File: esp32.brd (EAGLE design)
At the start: 59.2 x 57.2 mm, 14 parts, among them IC1 LM1117IMPX-3.3, U1 ESP32MOD

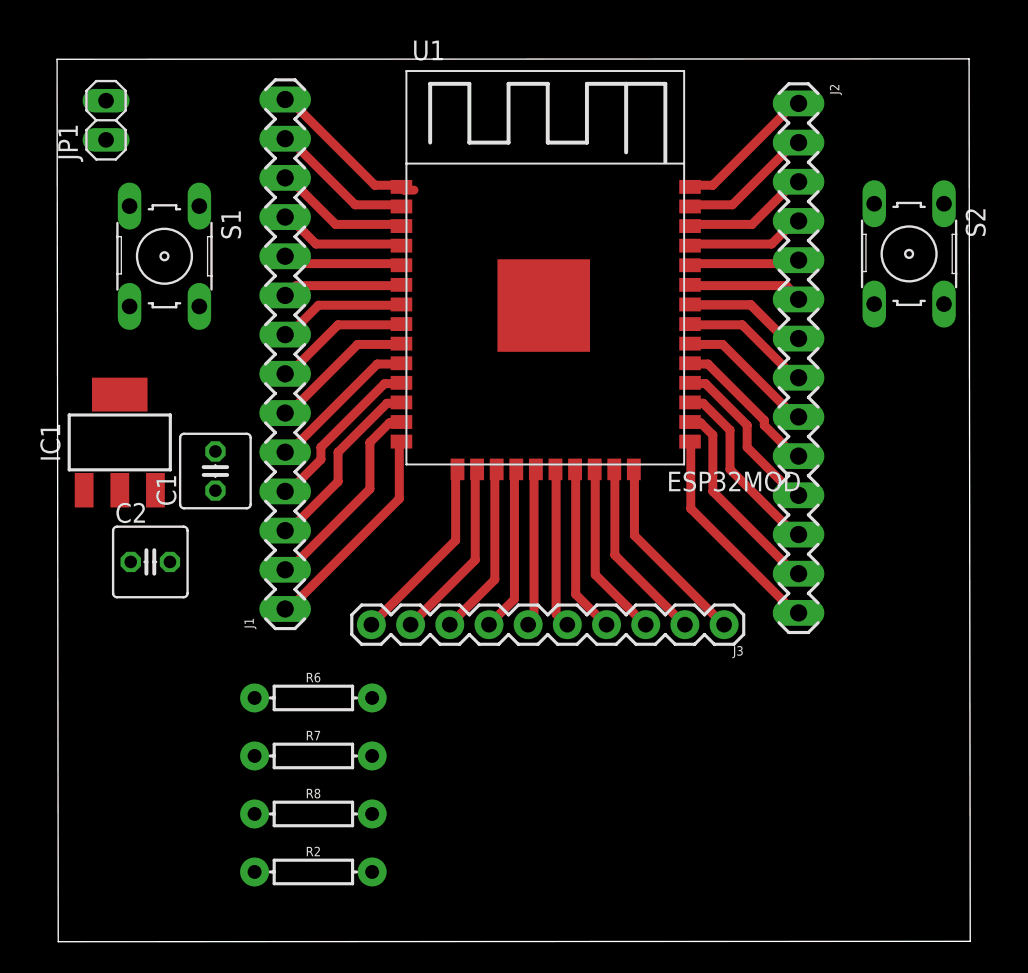
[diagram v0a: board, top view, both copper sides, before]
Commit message: updated track and placing of AMS117 modified, peripheral: NA
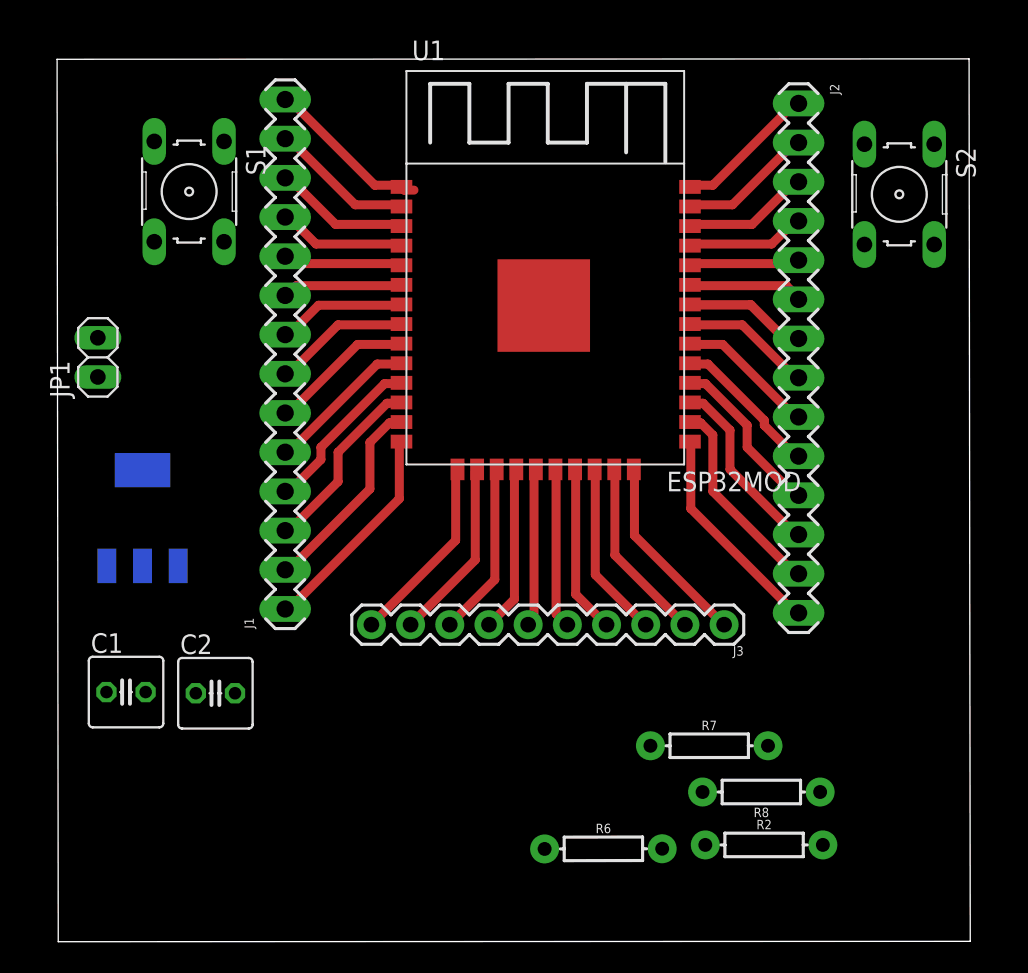
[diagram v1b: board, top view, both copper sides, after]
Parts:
- moved R2 29.3 mm to (58.7, 29.2)
- moved R8 29.1 mm to (58.5, 32.6), turned to 180 degrees
- moved R7 25.7 mm to (55.2, 35.6)
- moved R6 21.2 mm to (48.3, 28.9), turned to 0.1 degrees
- moved C1 15.5 mm to (17.4, 39.1), turned to 0 degrees
- moved JP1 15.4 mm to (15.5, 60.8)
- moved C2 9.50 mm to (23.2, 39.0)
- moved IC1 5.12 mm to (18.4, 50.3), flipped to the bottom
- moved S1 4.49 mm to (21.5, 71.5)
- moved S2 3.91 mm to (67.5, 71.3)
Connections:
- removed net N$28: J2.14, U1.25
- removed net N$4: J1.13, U1.2
- net N$5: now also J2.14, U1.25
- net VCC1: now also IC1.TAB, J1.13, U1.2
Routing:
- net N$5: track 0.00 -> 14.2 mm
- net N$28: track 14.2 -> 0.00 mm
- net VCC1: track 0.00 -> 9.35 mm
- net N$4: track 9.35 -> 0.00 mm
